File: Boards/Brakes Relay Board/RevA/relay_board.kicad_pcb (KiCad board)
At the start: 2 copper layers, 15 parts, among them J1 Screw_Terminal_01x04, J2 Screw_Terminal_01x04, J3 Screw_Terminal_01x04, J4 Screw_Terminal_01x04, J5 Conn_02x10_Counter_Clockwise, J6 Conn_02x12_Counter_Clockwise, J7 Screw_Terminal_01x04, U1 ALQ105, U2 ALQ105, U3 ALQ105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

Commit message: Relay Board RevA Rough PCB
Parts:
- added REF**: MountingHole_2.7mm_M2.5, MountingHole:MountingHole_2.7mm_M2.5, F.Cu at (202.5, 98.0)
- moved J6 342.2 mm to (239.5, 84.0)
- moved D1 330.2 mm to (235.0, 123.5)
- moved R1 325.3 mm to (230.1, 123.5)
- moved U5 295.5 mm to (215.2, 72.7)
- moved U6 282.9 mm to (228.7, 72.5)
- moved J2 279.2 mm to (189.7, 120.5)
- moved U4 277.7 mm to (234.5, 101.1)
- moved U2 261.6 mm to (177.1, 100.8), turned to 90 degrees
- moved J5 260.1 mm to (163.0, 86.6)
- moved J3 252.6 mm to (206.4, 120.3)
- moved J1 247.9 mm to (173.1, 120.7)
- moved U1 239.4 mm to (204.8, 102.9), turned to 90 degrees
- moved J4 239.1 mm to (199.3, 75.9), turned to 180 degrees
- moved U3 231.7 mm to (177.4, 87.6), turned to 90 degrees
- moved J7 198.7 mm to (182.6, 75.9), turned to 180 degrees
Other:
- board outline added: 85 x 56 mm

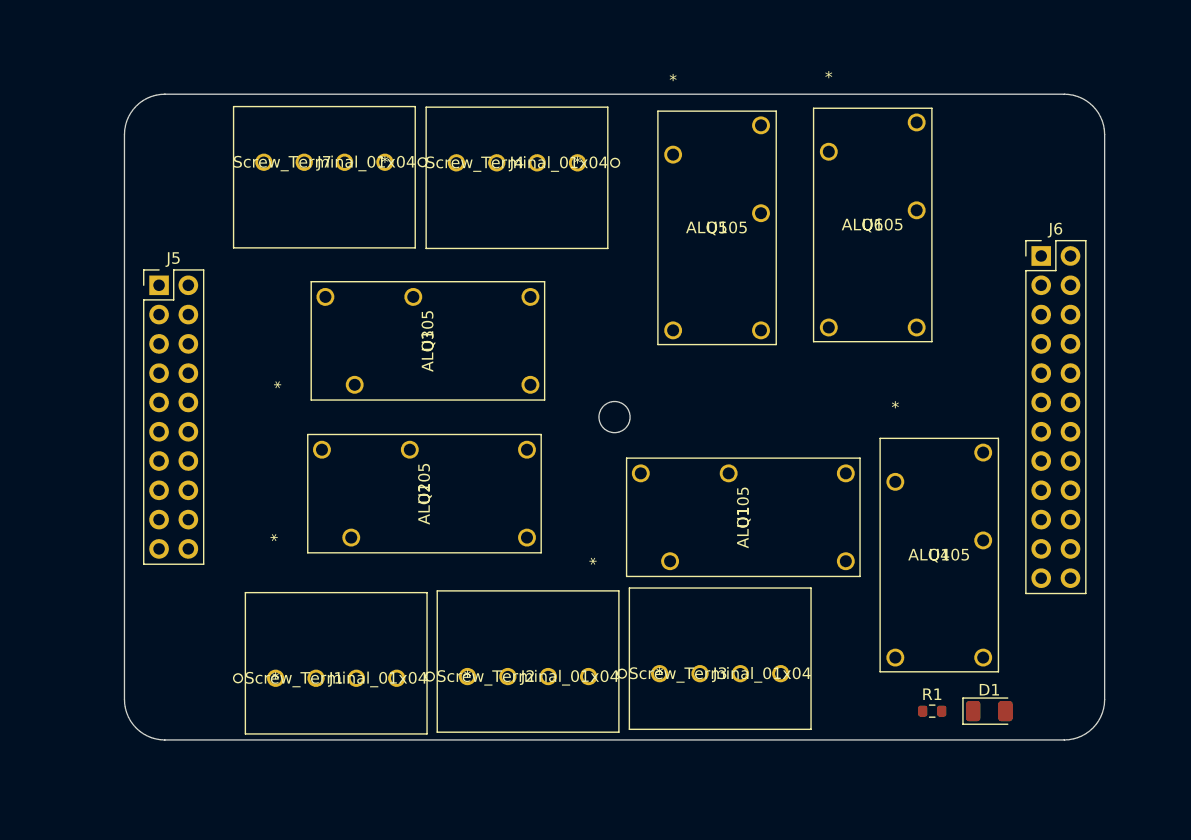
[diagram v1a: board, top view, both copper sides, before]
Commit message: Created Design File for Relay Board Rev A
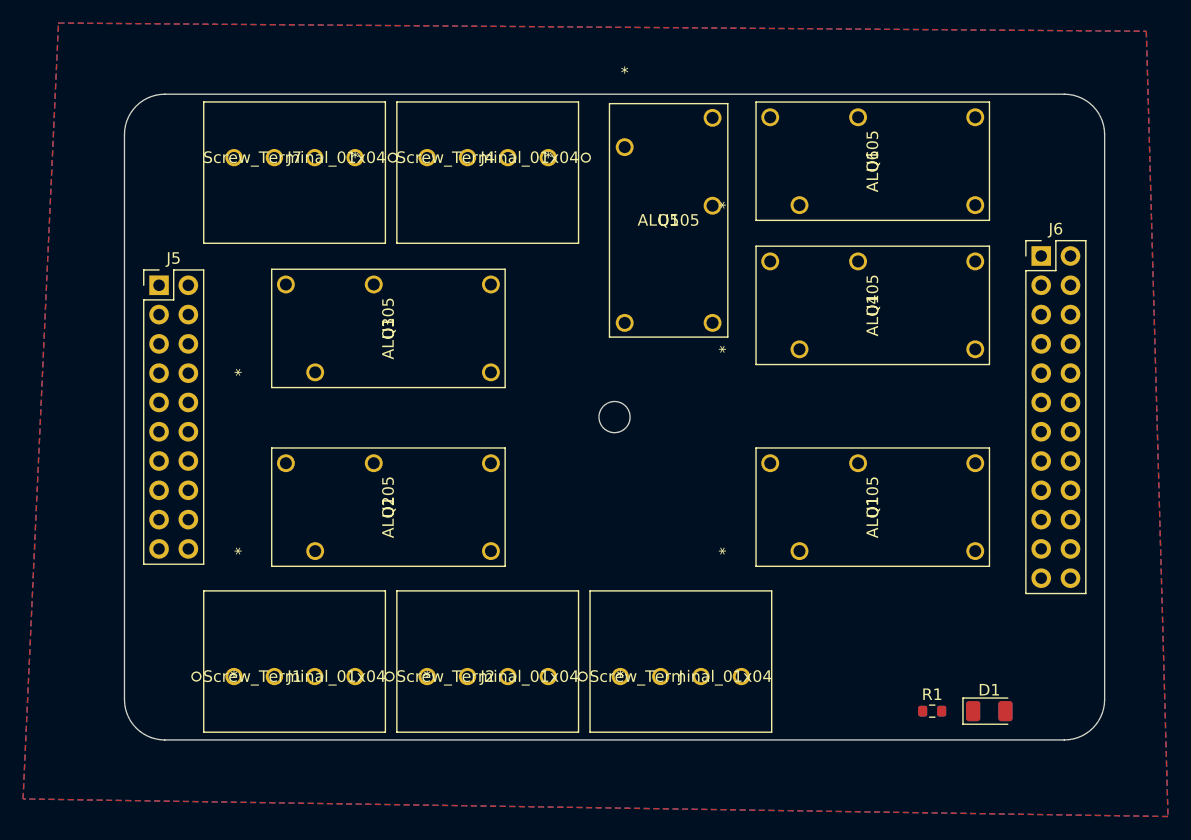
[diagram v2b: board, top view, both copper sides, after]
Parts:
- removed J3: Screw_Terminal_01x04, BAJA-4PIN:1984989
- added J: Screw_Terminal_01x04, BAJA-4PIN:1984989, F.Cu at (203.0, 120.5)
- moved U4 24.8 mm to (216.0, 84.5), turned to 90 degrees
- moved U6 12.7 mm to (216.0, 72.0), turned to 90 degrees
- moved U1 11.3 mm to (216.0, 102.0)
- moved U5 4.25 mm to (211.0, 72.0)
- moved J1 3.62 mm to (169.5, 120.5)
- moved U3 3.59 mm to (174.0, 86.5)
- moved J2 3.50 mm to (186.2, 120.5)
- moved U2 3.34 mm to (174.0, 102.0)
- moved J7 2.62 mm to (180.0, 75.5)
- moved J4 2.58 mm to (196.8, 75.5)
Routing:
- added copper zone on B.Cu, net /GND
- added copper zone on F.Cu, net /GND

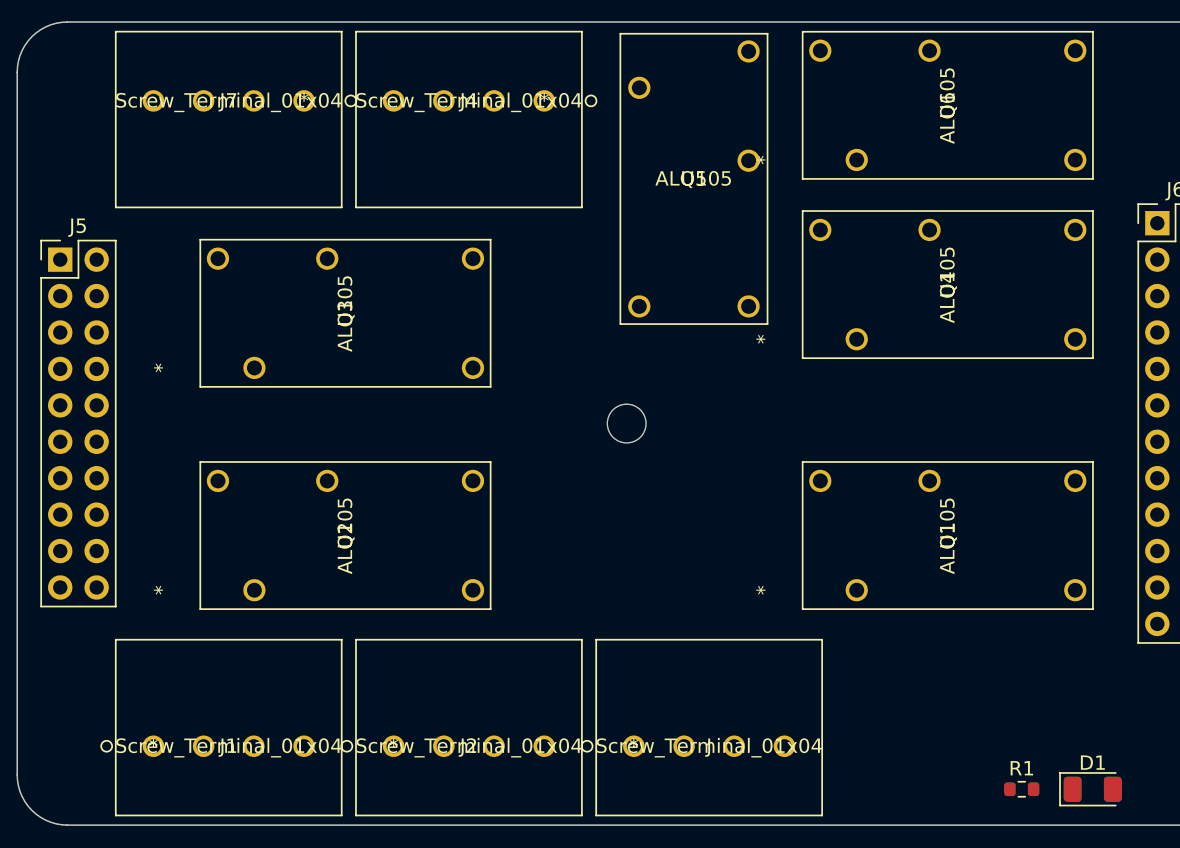
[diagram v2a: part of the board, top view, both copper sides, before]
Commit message: Added Screw Terminal Labels for Relay Board Rev a
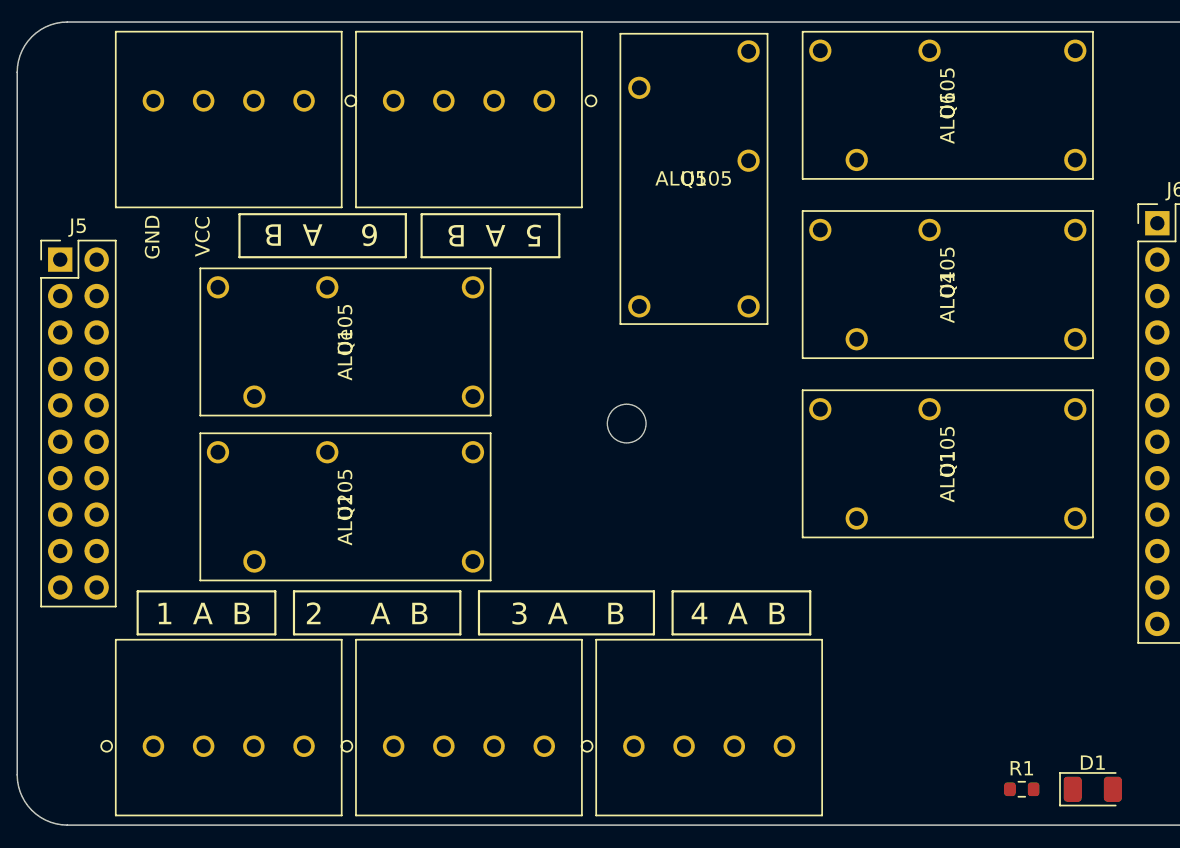
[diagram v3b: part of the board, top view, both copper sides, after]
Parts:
- moved U1 5.00 mm to (216.0, 97.0)
- moved U2 2.00 mm to (174.0, 100.0)
- moved Ue 2.00 mm to (174.0, 88.5)
- renumbered U3 to Ue
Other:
- board text added: "1 A B"
- board text added: "2 A B"
- board text added: "3 A B"
- board text added: "4 A B"
- board text added: "5 A B"
- board text added: "6 A B"
- board text added: "GND"
- board text added: "JLCJLCJLCJLC"
- board text added: "SDAQ SPDT Relay Board Revision A Samuel Grosser (215) 516-9799 RIT BAJA"
- board text added: "VCC"

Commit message: Relay Board Rev A Complete
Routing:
- net /VCC: track 0.00 -> 112.4 mm
- net /R5: track 0.00 -> 85.6 mm
- net /R0: track 0.00 -> 79.0 mm
- net /Ch1: track 0.00 -> 67.2 mm
- net /Ch3A: track 0.00 -> 67.0 mm
- net /R3: track 0.00 -> 57.3 mm
- net /Ch3B: track 0.00 -> 55.7 mm
- net /Ch1A: track 0.00 -> 52.7 mm
- net /R2: track 0.00 -> 52.5 mm
- net /Ch4A: track 0.00 -> 49.8 mm
- net /Ch1B: track 0.00 -> 48.6 mm
- net /Ch3: track 0.00 -> 48.2 mm
- net /Ch6B: track 0.00 -> 45.5 mm
- net /Ch4B: track 0.00 -> 45.4 mm
- net /Ch2A: track 0.00 -> 43.8 mm
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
